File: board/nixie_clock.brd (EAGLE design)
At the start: 115 x 55.2 mm, 47 parts, among them U1 AMS1117-5.0, U2 SN74141N

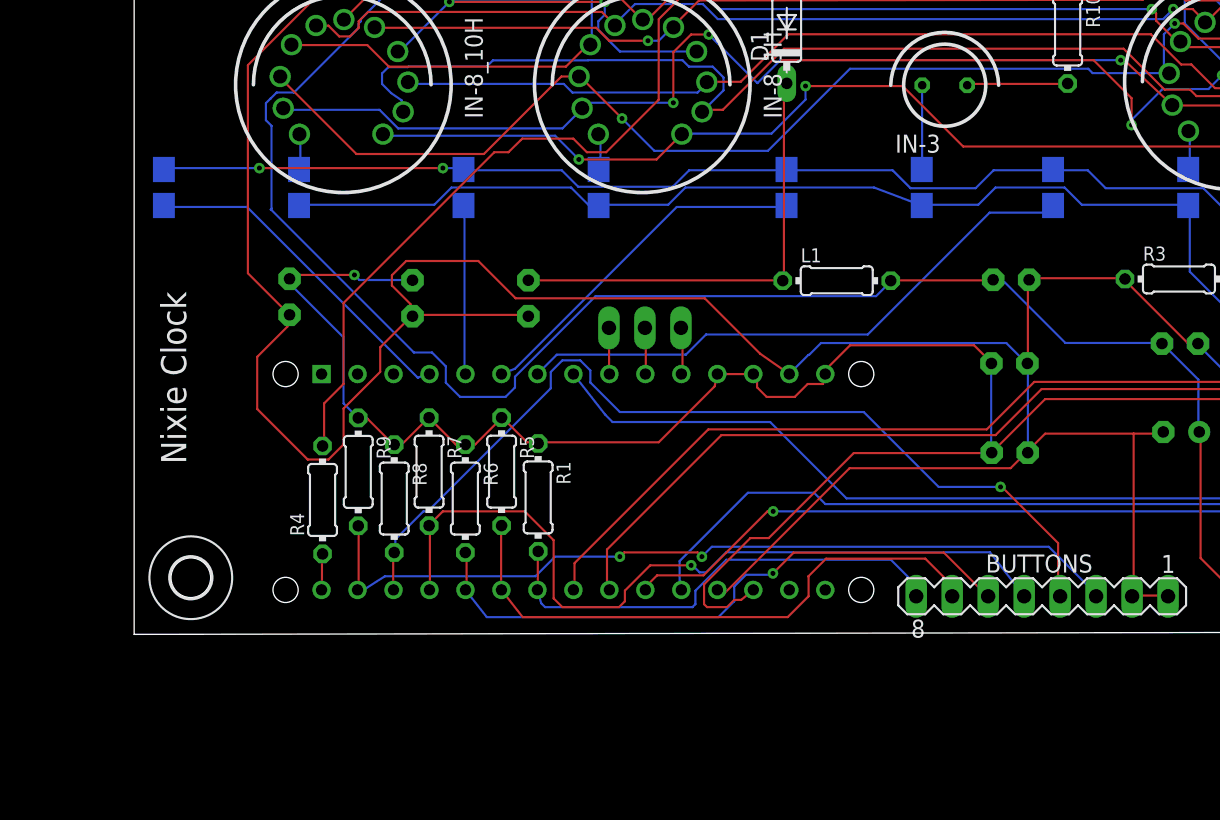
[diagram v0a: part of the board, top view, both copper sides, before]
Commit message: added button to D13
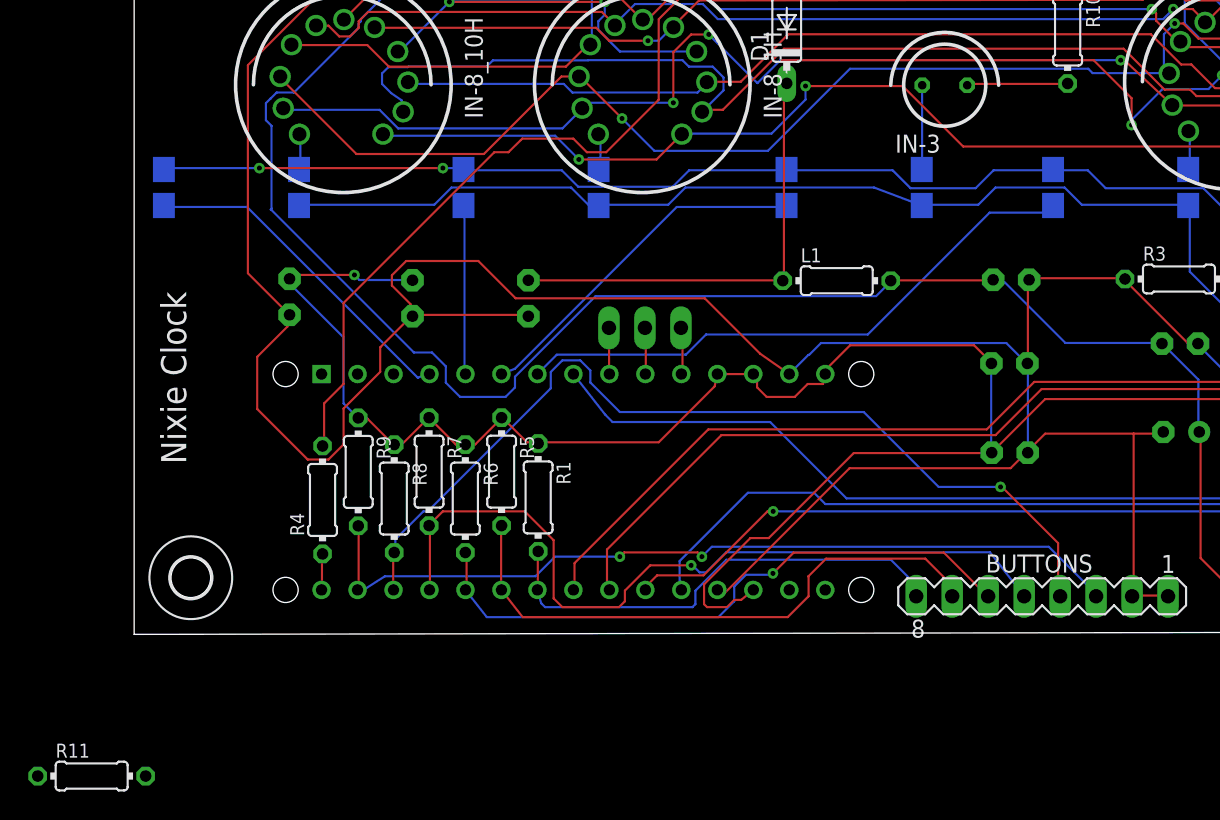
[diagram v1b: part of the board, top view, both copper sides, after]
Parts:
- added R11: 22k, rcl:0204/7
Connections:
- new net N$4: ARDUINO_NANO1.1, BUTTONS.2, R11.2
- net +5V: now also R11.1
- net GND: no longer BUTTONS.2
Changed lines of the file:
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@@
 <setting verticaltext="up"/>
 </settings>
-<grid distance="1" unitdist="mm" unit="mm" style="lines" multiple="1" display="yes" altdistance="0.1" altunitdist="mm" altunit="mm"/>
+<grid distance="0.999999999" unitdist="mm" unit="mm" style="lines" multiple="1" display="yes" altdistance="0.0999999999" altunitdist="mm" altunit="mm"/>
 <layers>
 <layer number="1" name="Top" color="4" fill="1" visible="yes" active="yes"/>
@@
 <attribute name="VALUE" x="16.075" y="47.16" size="1.778" layer="28" ratio="10" rot="MR90"/>
 </element>
+<element name="R11" library="rcl" library_urn="urn:adsk.eagle:library:334" package="0204/7" package3d_urn="urn:adsk.eagle:package:23498/2" value="22k" x="-3" y="-10" smashed="yes">
+<attribute name="NAME" x="-5.54" y="-8.7046" size="0.9906" layer="25" ratio="10"/>
+<attribute name="POPULARITY" value="79" x="-3" y="-10" size="1.778" layer="27" display="off"/>
+<attribute name="SPICEPREFIX" value="R" x="-3" y="-10" size="1.778" layer="27" display="off"/>
+<attribute name="VALUE" x="-4.6256" y="-10.4826" size="0.9906" layer="27" ratio="10"/>
+</element>
 </elements>
 <signals>
@@
 <contactref element="L1" pad="1"/>
 <contactref element="C1" pad="1"/>
-<wire x1="45.8724" y1="38.7096" x2="45.8724" y2="24.9936" width="0.1524" layer="1"/>
+<wire x1="45.8724" y1="25" x2="45.8724" y2="38.7096" width="0.1524" layer="1"/>
 <wire x1="46.0248" y1="38.862" x2="45.8724" y2="38.7096" width="0.1524" layer="1"/>
-<wire x1="45.8724" y1="24.9936" x2="45.79" y2="24.97" width="0.1524" layer="1"/>
 <wire x1="46.0248" y1="38.862" x2="46.07" y2="38.9" width="0.1524" layer="1"/>
 <wire x1="45.72" y1="24.9936" x2="27.8892" y2="24.9936" width="0.1524" layer="1"/>
 <wire x1="27.8892" y1="24.9936" x2="27.83" y2="25" width="0.1524" layer="1"/>
 <wire x1="45.72" y1="24.9936" x2="45.79" y2="24.97" width="0.1524" layer="1"/>
+<wire x1="45.79" y1="24.97" x2="45.8424" y2="24.97" width="0.1524" layer="1"/>
+<wire x1="45.8424" y1="24.97" x2="45.8724" y2="25" width="0.1524" layer="1"/>
 </signal>
 <signal name="GND">
@@
 <contactref element="BUZZER" pad="-"/>
 <contactref element="BUTTONS" pad="1"/>
-<contactref element="BUTTONS" pad="2"/>
 <contactref element="R10" pad="1"/>
 <contactref element="J1" pad="2"/>
@@
 <wire x1="63.0936" y1="12.954" x2="63.08" y2="12.83" width="0.1524" layer="1"/>
 <wire x1="70.5612" y1="14.1732" x2="70.5612" y2="2.7432" width="0.1524" layer="1"/>
-<wire x1="70.5612" y1="2.7432" x2="70.45" y2="2.69" width="0.1524" layer="1"/>
 <wire x1="27.7368" y1="22.5552" x2="19.6596" y2="22.5552" width="0.1524" layer="1"/>
 <wire x1="19.6596" y1="22.5552" x2="19.65" y2="22.46" width="0.1524" layer="1"/>
@@
 <wire x1="43.71" y1="18.38" x2="43.9761625" y2="18.1138375" width="0.1524" layer="1"/>
 <wire x1="43.9761625" y1="18.1138375" x2="43.9761625" y2="17.4410375" width="0.1524" layer="1"/>
+<contactref element="R11" pad="1"/>
+<wire x1="-6.81" y1="-10" x2="15.82" y2="15.28" width="0" layer="19" extent="1-1"/>
 </signal>
 <signal name="200V">
@@
 <via x="94.7" y="24.8" extent="1-16" drill="0.35"/>
 </signal>
+<signal name="N$4">
+<contactref element="R11" pad="2"/>
+<contactref element="BUTTONS" pad="2"/>
+<contactref element="ARDUINO_NANO1" pad="1"/>
+<wire x1="13.23" y1="18.38" x2="70.45" y2="2.69" width="0" layer="19" extent="1-1"/>
+<wire x1="0.81" y1="-10" x2="13.23" y2="18.38" width="0" layer="19" extent="1-1"/>
+</signal>
 </signals>

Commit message: finalized board component layout
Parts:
- removed J1: (no value), con-jack:DCJ0303
- added INPUT: 22-23-2021, con-molex:22-23-2021
- SHNT: value (none) -> 22-23-2021; device switch:320-916 -> con-molex:22-23-2021
- moved R11 84.4 mm to (76.0, 19.7), turned to 270 degrees
- moved R1 66.1 mm to (94.0, 18.4)
- moved R4 66.0 mm to (78.8, 18.0)
- moved R7 66.0 mm to (86.3, 19.7)
- moved ARDUINO_NANO1 66.0 mm to (99.0, 18.8)
- moved R6 66.0 mm to (88.8, 18.2)
- moved R8 65.9 mm to (83.8, 17.9)
- moved R9 65.9 mm to (81.2, 19.7)
- moved R5 65.9 mm to (91.3, 19.6)
- moved SHNT 51.9 mm to (51.5, 4.70), flipped to the top, turned to 0 degrees
- moved RTC 49.8 mm to (85.0, 30.5), flipped to the top, turned to 180 degrees
- moved C3 43.7 mm to (41.9, 17.1), turned to 90 degrees
- moved L3 39.7 mm to (41.8, 7.87), turned to 270 degrees
- moved BUZZER 39.3 mm to (63.5, 9.22), turned to 180 degrees
- moved C4 38.3 mm to (49.2, 27.1), turned to 90 degrees
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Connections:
- net +12V: now also SHNT.2; no longer SHNT.1, SHNT.3
- net GND: now also INPUT.2, SHNT.1; no longer J1.1, J1.2, SHNT.2
- net N$1: now also INPUT.1; no longer J1.3
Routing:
- net GND: track 343.6 -> 0.00 mm
- net K4: track 197.0 -> 0.00 mm, vias 5 -> 0
- net +5V: track 177.9 -> 0.00 mm, vias 1 -> 0
- net K9: track 158.5 -> 0.00 mm, vias 3 -> 0
- net K2: track 146.8 -> 0.00 mm
- net +12V: track 142.8 -> 0.00 mm
- net K5: track 137.5 -> 0.00 mm, vias 3 -> 0
- net K8: track 133.7 -> 0.00 mm, vias 1 -> 0
- net K6: track 125.4 -> 0.00 mm, vias 2 -> 0
- net K0: track 117.3 -> 0.00 mm, vias 5 -> 0
- net K7: track 113.4 -> 0.00 mm, vias 3 -> 0
- net K1: track 107.4 -> 0.00 mm, vias 2 -> 0
- net K3: track 104.8 -> 0.00 mm, vias 1 -> 0
- net N$5: track 103.6 -> 0.00 mm, vias 1 -> 0
- net N$16: track 95.4 -> 0.00 mm, vias 3 -> 0
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- added copper zone on layer 16, net GND
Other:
- board size 115 x 55.2 mm -> 130 x 79 mm

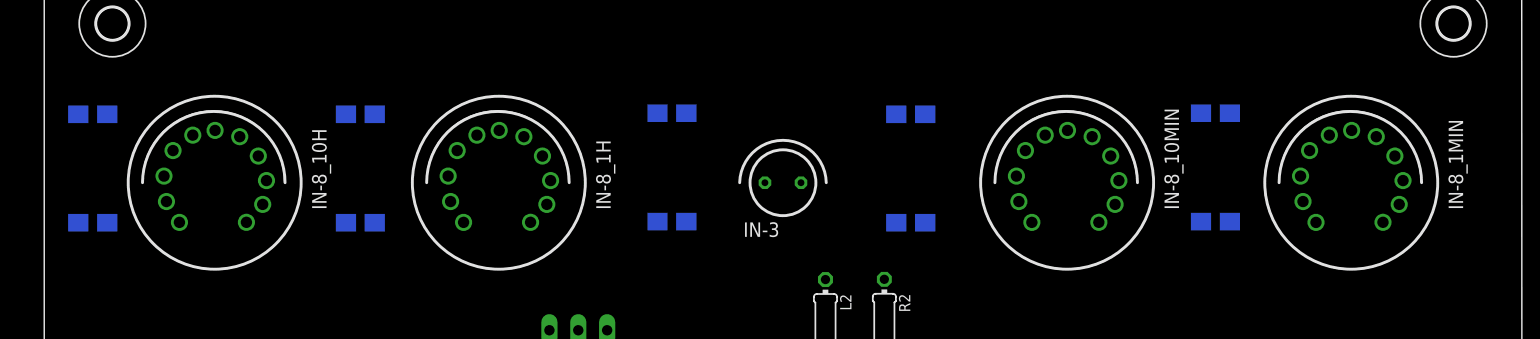
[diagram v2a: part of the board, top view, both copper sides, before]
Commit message: moved the tubes towards the center
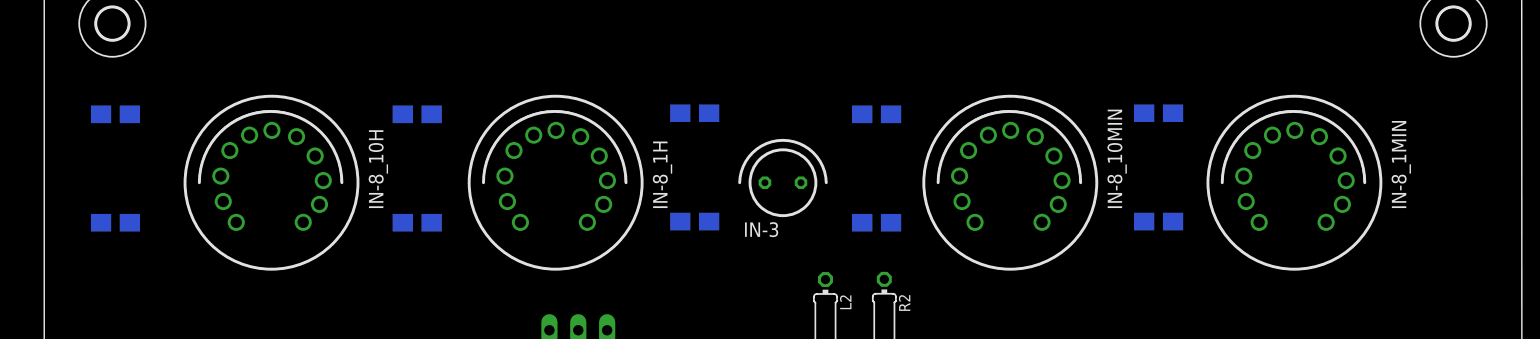
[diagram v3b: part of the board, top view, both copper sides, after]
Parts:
- moved IN-8_10H 5.00 mm to (20.0, 59.0)
- moved IN-8_10MIN 5.00 mm to (85.0, 59.0)
- moved IN-8_1H 5.00 mm to (45.0, 59.0)
- moved IN-8_1MIN 5.00 mm to (110.0, 59.0)
- moved OK2 5.00 mm to (32.8, 60.2)
- moved OK5 5.00 mm to (98.0, 60.4)
- moved OK4 3.00 mm to (73.2, 60.2)
- moved OK1 2.00 mm to (6.27, 60.2)
- moved OK3 2.00 mm to (57.2, 60.4)

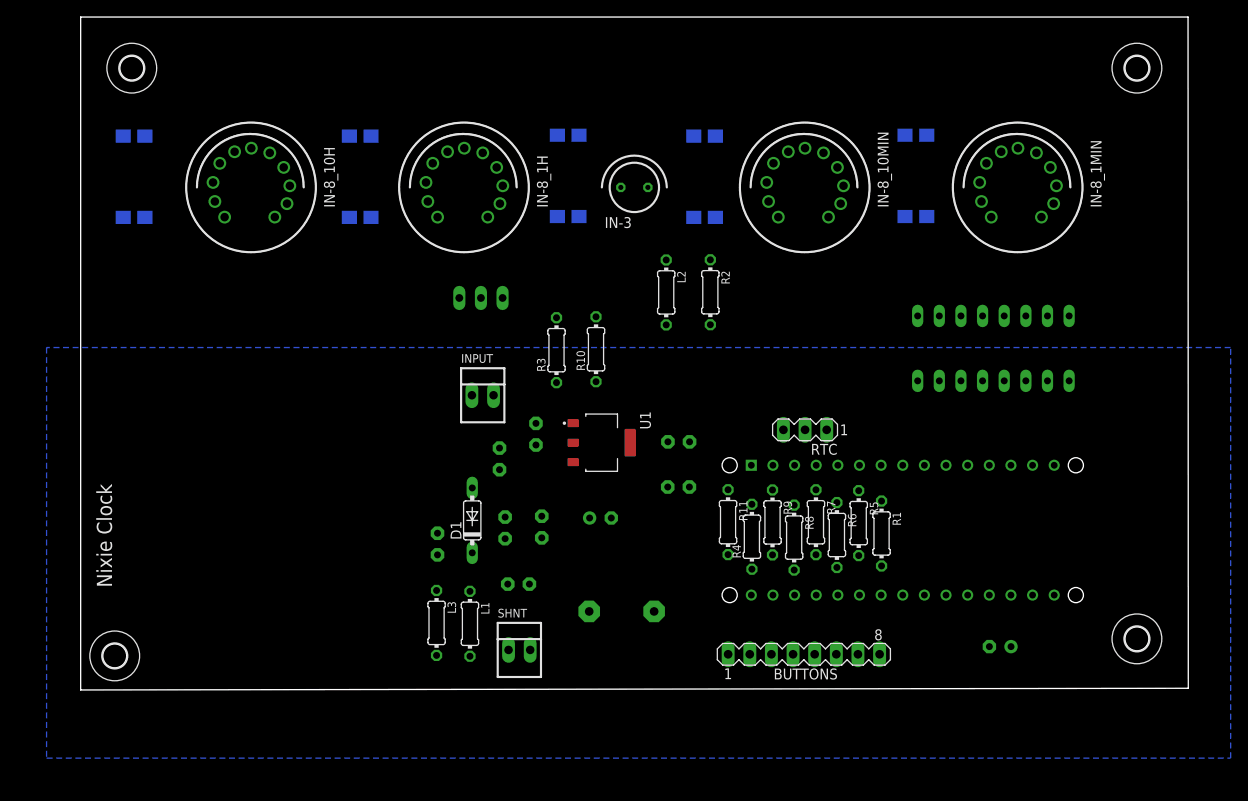
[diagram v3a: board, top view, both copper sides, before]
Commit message: ran autorouter with jlcpcb capabilities
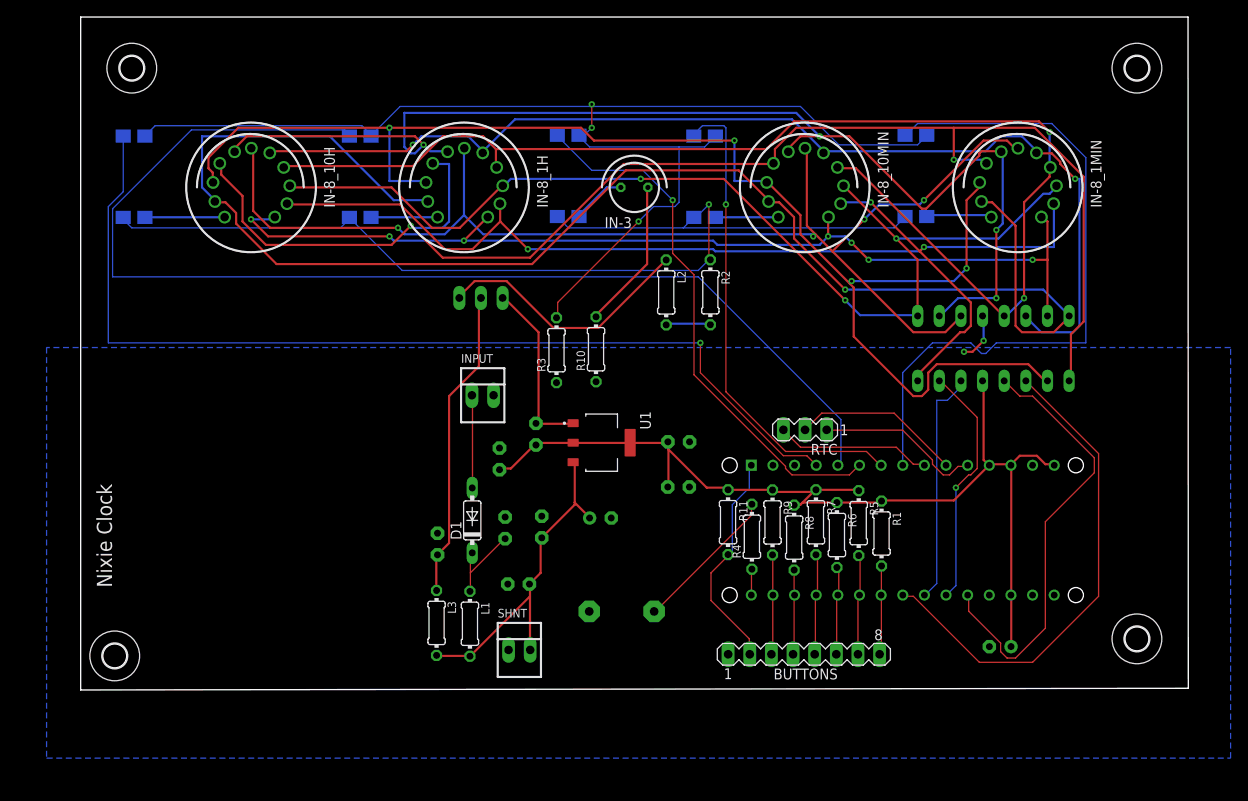
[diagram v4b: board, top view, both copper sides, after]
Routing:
- net K0: track 0.00 -> 179.6 mm, vias 0 -> 1
- net K8: track 0.00 -> 166.0 mm, vias 0 -> 2
- net K9: track 0.00 -> 163.2 mm, vias 0 -> 4
- net K4: track 0.00 -> 146.9 mm, vias 0 -> 2
- net N$16: track 0.00 -> 146.6 mm, vias 0 -> 3
- net K6: track 0.00 -> 145.5 mm, vias 0 -> 4
- net K7: track 0.00 -> 141.3 mm, vias 0 -> 4
- net N$26: track 0.00 -> 138.1 mm
- net K2: track 0.00 -> 135.5 mm, vias 0 -> 3
- net K5: track 0.00 -> 128.0 mm, vias 0 -> 2
- net N$5: track 0.00 -> 126.0 mm, vias 0 -> 1
- net K3: track 0.00 -> 125.2 mm, vias 0 -> 3
- net +5V: track 0.00 -> 118.8 mm
- net K1: track 0.00 -> 117.4 mm, vias 0 -> 7
- net N$15: track 0.00 -> 116.1 mm, vias 0 -> 1
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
